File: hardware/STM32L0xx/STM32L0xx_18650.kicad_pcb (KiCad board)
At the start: 4 copper layers, 108.4 x 16 mm, 51 parts, among them J1 SWD, J2 Battery, J3 GPIO, J4 USB_B_Micro, J5 Power, J6 LEDs, J7 GPIO, Q1 BSS806N, Q2 BSS806N, Q3 BSS806N, Q4 BSS806N, SW1 Mode, SW2 Power, U1 STM32L072CBTx, U2 AP2210-3.3TRG1, U3 MCP73831T-2ACI/OT, Y1 32.768kHz

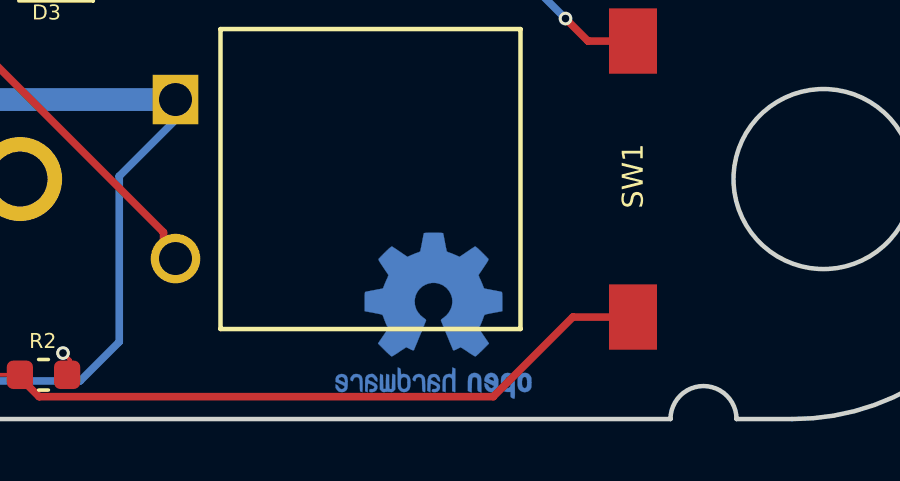
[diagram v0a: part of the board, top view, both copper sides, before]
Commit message: Rename LitFist to Thunder Pack
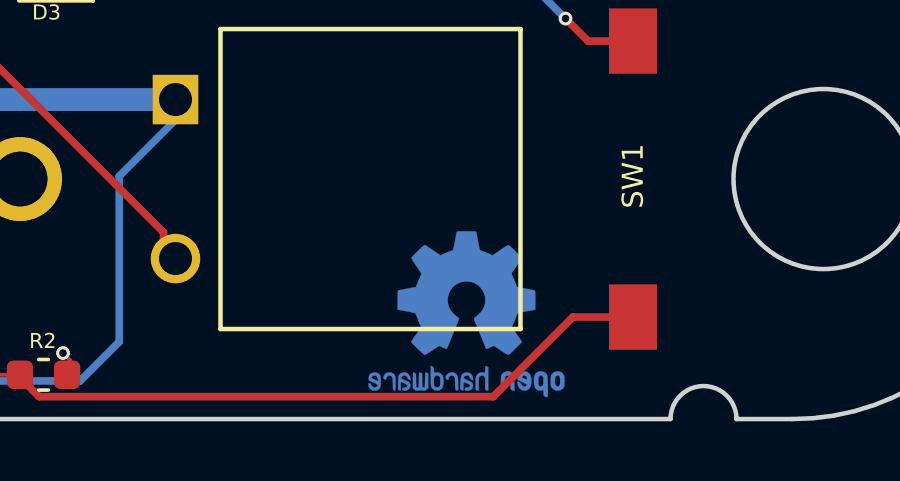
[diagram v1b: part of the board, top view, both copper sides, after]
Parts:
- moved REF** 1.10 mm to (147.6, 104.5)
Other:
- board text added: "Thunder Pack"
- board text removed: "pArm board"
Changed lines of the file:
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@@
-(kicad_pcb (version 20171130) (host pcbnew "(5.1.0-0)")
+(kicad_pcb (version 20171130) (host pcbnew "(5.1.4-0-10_14)")
   (general
     (thickness 1.6)
@@
   )
   (setup
-    (last_trace_width 0.254)
+    (last_trace_width 0.127)
     (user_trace_width 0.254)
     (user_trace_width 0.762)
@@
   )
   (module Symbol:OSHW-Logo2_7.3x6mm_Copper (layer B.Cu)
-    (at 146.5 104.55 180)
+    (at 147.6 104.5 180)
     (descr "Open Source Hardware Symbol")
     (tags "Logo Symbol OSHW")
@@
     (effects (font (size 0.5 0.5) (thickness 0.08)))
   )
-  (gr_text "v1\nJeremy Gillick" (at 146.375 99.3) (layer B.SilkS)
+  (gr_text "v1\nJeremy Gillick" (at 147.475 99.25) (layer B.SilkS)
     (effects (font (size 1.2 1.2) (thickness 0.12)) (justify mirror))
   )
-  (gr_text "pArm board" (at 146.3 96.2) (layer B.SilkS)
+  (gr_text "Thunder Pack" (at 147.4 96.15) (layer B.SilkS)
     (effects (font (size 1.5 1.5) (thickness 0.2)) (justify mirror))
   )

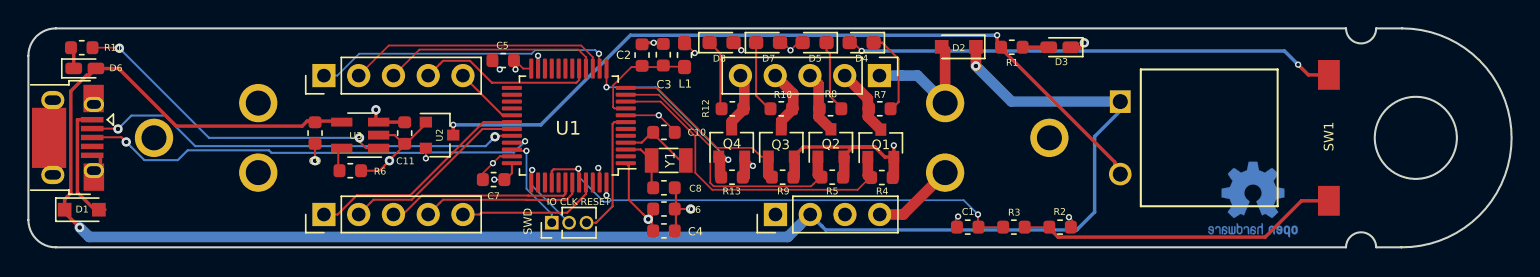
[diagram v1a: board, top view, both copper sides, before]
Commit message: Add a full 10-pin JTAG connector.
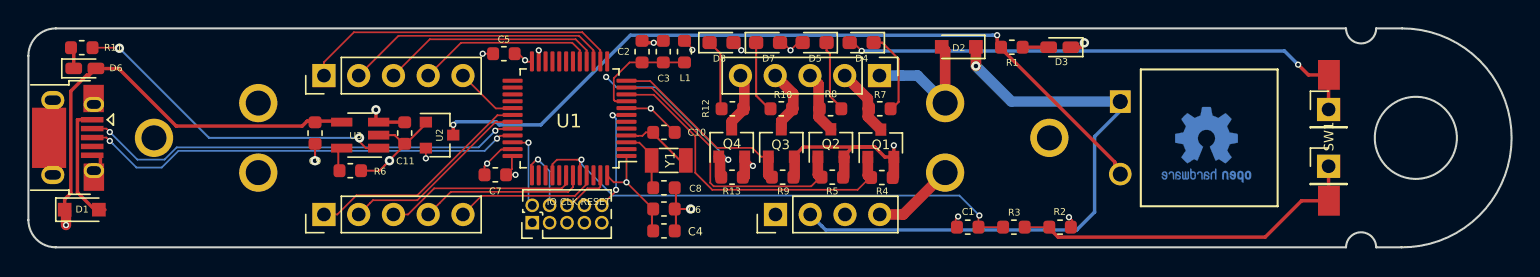
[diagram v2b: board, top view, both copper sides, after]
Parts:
- added J8: Conn_01x01, Connector_PinHeader_2.54mm:PinHeader_1x01_P2.54mm_Vertical, F.Cu at (153.1, 97.9)
- added J9: Conn_01x01, Connector_PinHeader_2.54mm:PinHeader_1x01_P2.54mm_Vertical, F.Cu at (153.1, 102.1)
- J1: value SWD -> SW Debug; footprint Connector_PinHeader_1.27mm:PinHeader_1x03_P1.27mm_Vertical -> Connector_PinHeader_1.27mm:PinHeader_2x05_P1.27mm_Vertical
- L1: footprint Inductor_SMD:L_0603_1608Metric_Pad1.05x0.95mm_HandSolder -> Inductor_SMD:L_0603_1608Metric
- R1: value 330 -> 270
- U2: value AP2210-3.3TRG1 -> AP2210N-3.3TRG1
- moved REF** 5.25 mm to (144.2, 100.5)
- moved J1 1.42 mm to (94.9, 106.2)
- moved U1 0.53 mm to (97.7, 98.6)
- moved C5 0.50 mm to (92.8, 93.8)
- moved C7 0.37 mm to (92.2, 102.7)
- moved C2 0.25 mm to (103.0, 93.7)
- moved L1 0.25 mm to (106.0, 93.7)
- moved C3 0.22 mm to (104.5, 93.7)
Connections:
- J1 pad 1: /SWDIO -> +3V3
- J1 pad 2: /SWCLK -> /SWDIO
- J1 pad 3: /RESET -> GND
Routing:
- net GND: track 51.6 -> 54.6 mm, vias 14 -> 13
- net Net-(J9-Pad1): track 23.6 -> 26.1 mm
- net +3V3: track 52.6 -> 54.7 mm, vias 10 -> 9
- net /BUTTON: track 37.5 -> 39.4 mm
- net /PA4: track 22.1 -> 23.5 mm, vias 1 -> 0
- net /RESET: track 9.44 -> 8.14 mm, vias 0 -> 2
- net /PA6: track 15.9 -> 17.2 mm
- net /PA5: track 19.2 -> 20.5 mm
- net /SWDIO: track 7.12 -> 5.86 mm
- net /LED4: track 14.8 -> 13.8 mm
- net /USB_D+: track 33.5 -> 32.6 mm
- net /USB_D-: track 31.7 -> 32.6 mm
- net /PB6: track 14.0 -> 14.8 mm
- net /VUSB: track 130.4 -> 131.1 mm
- net /SWCLK: track 5.91 -> 6.44 mm
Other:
- board text added: "Created by Jeremy Gillick"
- board text added: "Thunder Pack v1"
- board text removed: "Thunder Pack"
- board text removed: "v1 Jeremy Gillick"

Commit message: Change to 32 pin package.
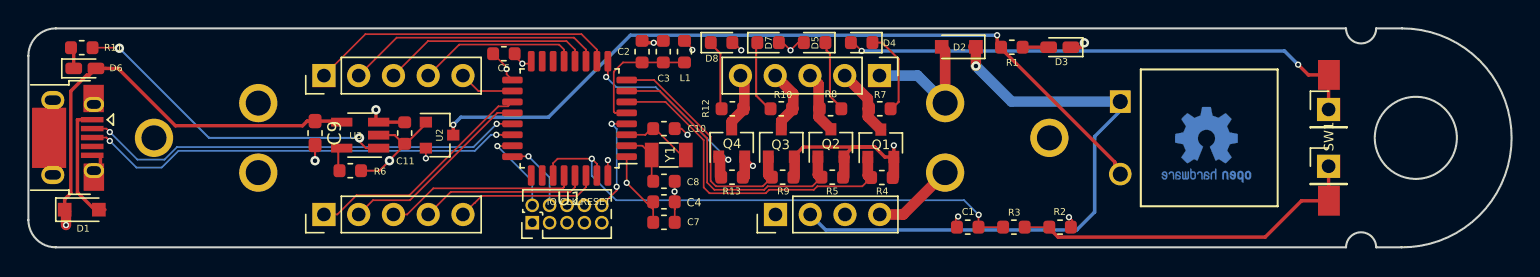
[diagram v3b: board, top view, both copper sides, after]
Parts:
- removed C6: 100nf, Capacitor_SMD:C_0603_1608Metric
- C9: footprint Capacitor_SMD:C_0603_1608Metric -> Capacitor_SMD:C_0603_1608Metric_Pad1.05x0.95mm_HandSolder
- D4, D5, D7, D8: footprint LED_SMD:LED_0603_1608Metric_Pad1.05x0.95mm_HandSolder -> LED_SMD:LED_0603_1608Metric
- U1: value STM32L072CBTx -> STM32L072KZTx; footprint Package_QFP:LQFP-48_7x7mm_P0.5mm -> Package_QFP:LQFP-32_7x7mm_P0.8mm
- moved C7 12.8 mm to (104.5, 106.2), turned to 0 degrees
- moved C4 2.12 mm to (104.5, 104.7)
- moved C8 0.48 mm to (104.5, 103.2)
- moved Y1 0.40 mm to (104.9, 101.2)
- moved C10 0.27 mm to (104.5, 99.3)
- turned C5 to 0 degrees
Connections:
- J7 pad 3: /PB6 -> /PB5
- J7 pad 4: /PB7 -> /PB6
- J7 pad 5: /PB8 -> /PB7
- U1 pad 10: /LED1 -> /PA4
- U1 pad 11: /LED2 -> /PA5
- U1 pad 12: /LED3 -> /PA6
- U1 pad 13: /LED4 -> /PA7
- U1 pad 14: /PA4 -> (no net)
- U1 pad 15: /PA5 -> (no net)
- U1 pad 16: /PA6 -> GND
- U1 pad 17: /PA7 -> +3V3
- U1 pad 18: (no net) -> /PA8
- U1 pad 19: (no net) -> /PA9
- U1 pad 2: (no net) -> Net-(C8-Pad1)
- U1 pad 20: (no net) -> /PA10
- U1 pad 21: (no net) -> /USB_D-
- U1 pad 22: (no net) -> /USB_D+
- U1 pad 23: GND -> /SWDIO
- U1 pad 24: +3V3 -> /SWCLK
- U1 pad 27: (no net) -> /BUTTON
- U1 pad 28: (no net) -> /PB5
- U1 pad 29: /PA8 -> /PB6
- U1 pad 3: Net-(C8-Pad1) -> Net-(C10-Pad1)
- U1 pad 30: /PA9 -> /PB7
- U1 pad 31: /PA10 -> /BUTTON
- U1 pad 32: /USB_D- -> GND
- U1 pad 4: Net-(C10-Pad1) -> /RESET
- U1 pad 5: (no net) -> Net-(C2-Pad1)
- U1 pad 6: (no net) -> /LED1
- U1 pad 7: /RESET -> /LED2
- U1 pad 8: GND -> /LED3
- U1 pad 9: Net-(C2-Pad1) -> /LED4
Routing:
- net /PB5: track 0.00 -> 14.8 mm
- net GND: track 54.6 -> 43.9 mm, vias 13 -> 12
- net /PB8: track 10.6 -> 0.00 mm
- net /LED3: track 14.2 -> 17.6 mm
- net +3V3: track 54.7 -> 51.8 mm, vias 9 -> 8
- net /PB6: track 14.8 -> 12.4 mm
- net /PA6: track 17.2 -> 15.4 mm
- net /PB7: track 12.2 -> 10.7 mm
- net /PA7: track 13.1 -> 11.9 mm
- net /LED4: track 13.8 -> 15.0 mm
- net Net-(C2-Pad1): track 8.24 -> 9.38 mm
- net /SWCLK: track 6.44 -> 5.41 mm
- net /PA4: track 23.5 -> 22.6 mm
- net /USB_D+: track 32.6 -> 33.4 mm
- net /VUSB: track 131.1 -> 131.8 mm
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
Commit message: Add top labels and cleanup.
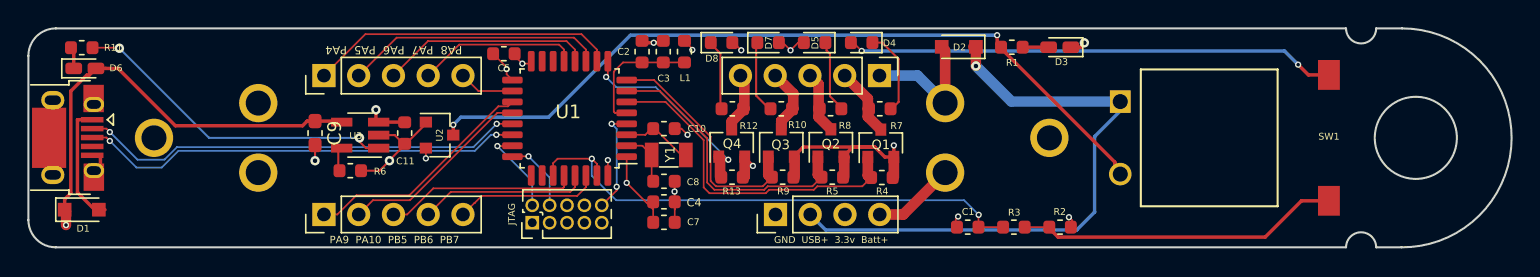
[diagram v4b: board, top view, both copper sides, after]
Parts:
- removed J8, J9: Conn_01x01, Connector_PinHeader_2.54mm:PinHeader_1x01_P2.54mm_Vertical
- removed REF**: OSHW-Logo2_7.3x6mm_Copper, Symbol:OSHW-Logo2_7.3x6mm_Copper
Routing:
- net +3V3: track 51.8 -> 49.3 mm
- net Net-(R2-Pad1): track 26.1 -> 23.6 mm
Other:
- board text added: "GND USB+ 3.3v Batt+"
- board text added: "JTAG"
- board text added: "PA8 PA7 PA6 PA5 PA4"
- board text added: "PA9 PA10 PB5 PB6 PB7"
- board text removed: "CLK"
- board text removed: "IO"
- board text removed: "RESET"

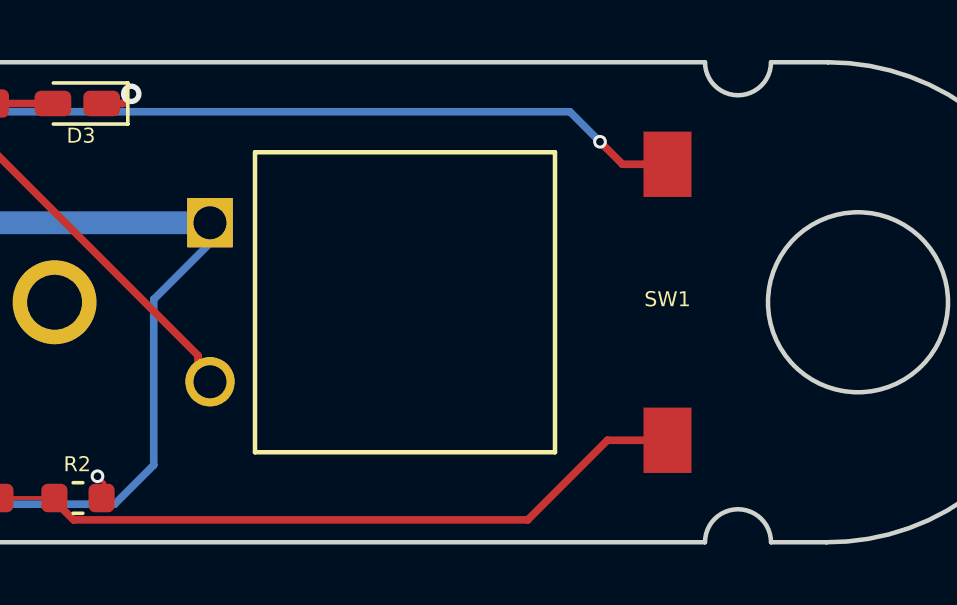
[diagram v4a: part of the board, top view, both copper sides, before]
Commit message: Use standard parts/symbols
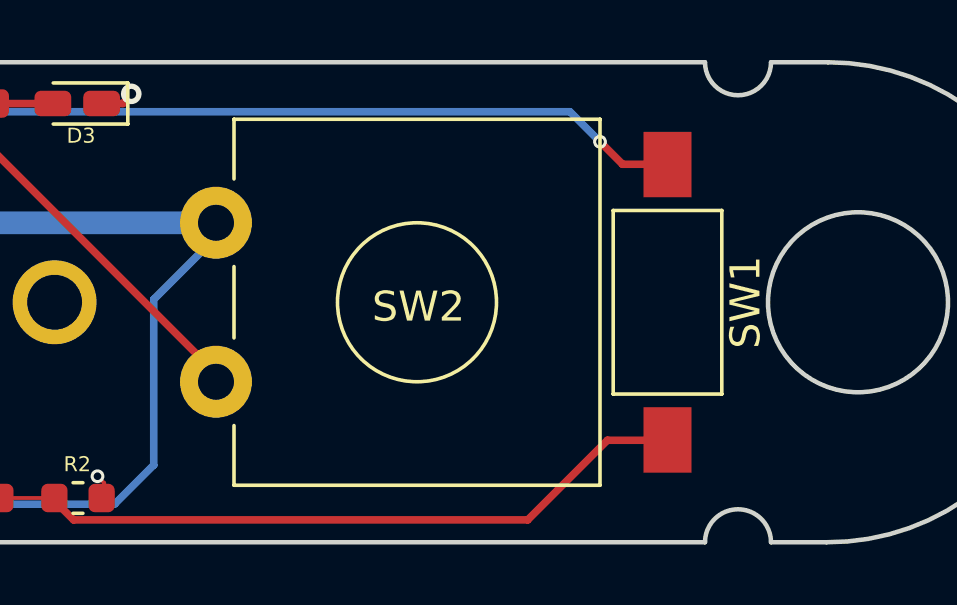
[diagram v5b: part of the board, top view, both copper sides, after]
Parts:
- SW1: footprint Jeremy:Switch_TE_FSMSM -> Button_Switch_SMD:SW_SPST_FSMSM
- SW2: footprint Jeremy:Switch_SPST_GPTS203211BR2 -> Button_Switch_THT:SW_CW_GPTS203211B
- moved SW2 6.83 mm to (138.1, 97.3), turned to 0 degrees
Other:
- board text added: "Thunder Pack"
- board text added: "rev 1a"
- board text removed: "Thunder Pack v1"

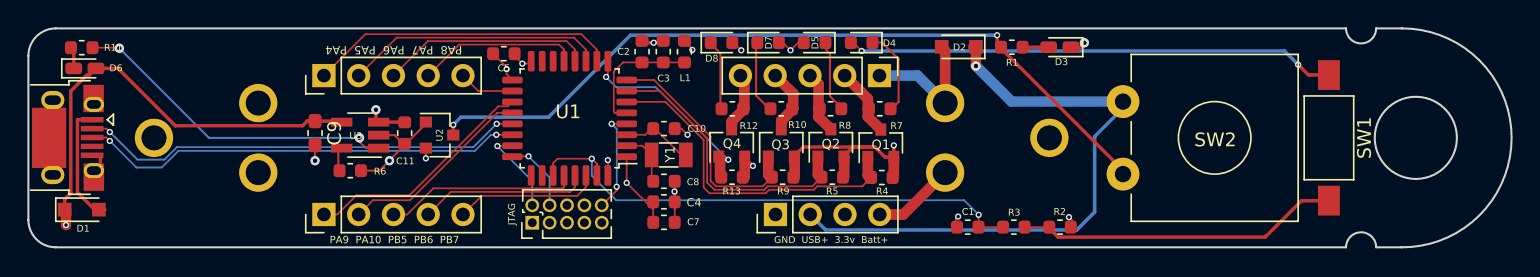
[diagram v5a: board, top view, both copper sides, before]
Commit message: Update charger IC (MCP73833-AMI_UN)
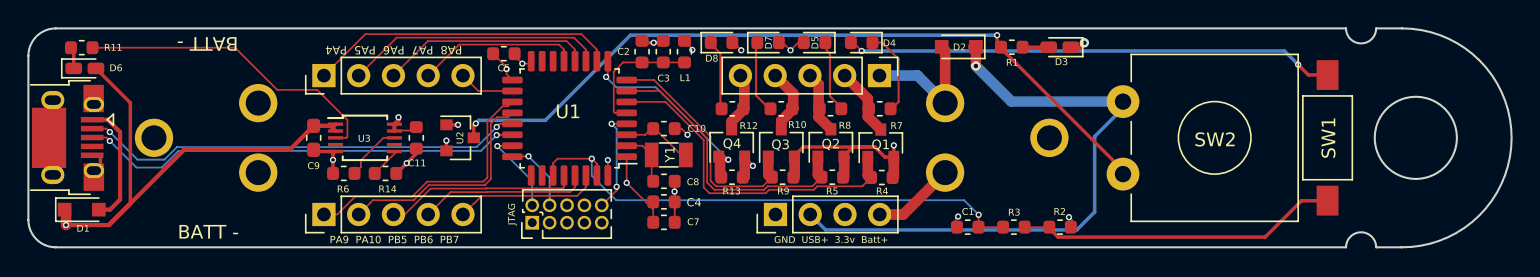
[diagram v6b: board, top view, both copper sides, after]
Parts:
- added R14: 10k, Resistor_SMD:R_0603_1608Metric, F.Cu at (81.2, 102.6)
- C11: value 4.7uF -> 1uf
- C9: value 4.7uF -> 1uF
- R6: value 2k -> 1k
- U3: value MCP73831T-2ACI/OT -> MCP73833-AMI_UN; footprint Package_TO_SOT_SMD:SOT-23-5_HandSoldering -> Package_SO:TSSOP-10_3x3mm_P0.5mm
- moved R6 2.58 mm to (84.2, 102.6)
- moved U2 1.51 mm to (89.7, 100.0)
- moved C11 0.92 mm to (86.5, 100.0)
- moved U3 0.40 mm to (82.7, 100.0), turned to 0 degrees
- moved C9 0.36 mm to (79.0, 100.0)
- moved SW1 0.10 mm to (153.1, 100.0)
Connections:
- U3 pad 1: Net-(R11-Pad1) -> /VUSB
- U3 pad 2: GND -> /VUSB
- U3 pad 3: +BATT -> Net-(R11-Pad1)
- U3 pad 4: /VUSB -> (no net)
- U3 pad 5: Net-(R6-Pad1) -> GND
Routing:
- net /VUSB: track 131.8 -> 138.1 mm
- net +BATT: track 70.3 -> 64.7 mm
- net Net-(R14-Pad1): track 0.00 -> 4.33 mm
- net GND: track 43.9 -> 41.3 mm, vias 12 -> 13
- net /PA9: track 17.2 -> 19.6 mm
- net /PA10: track 14.3 -> 16.7 mm
- net /VIN: track 56.9 -> 55.4 mm
- net Net-(R11-Pad1): track 24.1 -> 23.0 mm, vias 2 -> 0
- net Net-(D1-Pad2): track 10.0 -> 11.1 mm
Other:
- board text added: "BATT -"
